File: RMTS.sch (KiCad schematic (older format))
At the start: 49 parts, among them J1 USB_B_Mini, J2 Programmer, J3 Screw_Terminal_01x03, J4 Screw_Terminal_01x04, J5 Screw_Terminal_01x02, J6 Screw_Terminal_01x02, J8 CONN_03, Q1 PMV20ENR, U1 ADP2108AUJ-3.3, U2 MK20DX256VLH7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

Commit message: Fixed rescued symbols
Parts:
- JP1: symbol RMTS-rescue:XBEE-SparkFun-RF -> SparkFun-RF:XBEE
- U2: symbol RMTS-rescue:MK20DX256VLH7-Mine -> Mine:MK20DX256VLH7
- U3: symbol RMTS-rescue:ADS1219-Mine -> Mine:ADS1219
- U4: symbol RMTS-rescue:MCP6N11-Mine -> Mine:MCP6N11
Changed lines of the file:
@@
 $EndDescr
 $Comp
-L RMTS-rescue:MK20DX256VLH7-Mine U2
+L Mine:MK20DX256VLH7 U2
 U 1 1 5D344F89
 P 9450 1500
@@
 Connection ~ 6800 4100
 $Comp
-L RMTS-rescue:ADS1219-Mine U3
+L Mine:ADS1219 U3
 U 1 1 5D3AE65D
 P 3650 6800
@@
 $EndComp
 $Comp
-L RMTS-rescue:MCP6N11-Mine U4
+L Mine:MCP6N11 U4
 U 1 1 5D4392E2
 P 3650 8100
@@
 $EndComp
 $Comp
-L RMTS-rescue:XBEE-SparkFun-RF JP1
+L SparkFun-RF:XBEE JP1
 U 1 1 5D38660F
 P 9500 7900

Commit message: Fixed broken header
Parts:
- J8: symbol RMTS-rescue:CONN_03-SparkFun-Connectors -> SparkFun-Connectors:CONN_03
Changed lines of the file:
@@
 $EndComp
 $Comp
-L RMTS-rescue:CONN_03-SparkFun-Connectors J8
+L SparkFun-Connectors:CONN_03 J8
 U 1 1 5D6FAE37
 P 12550 4900

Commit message: Fixed older microSD footprint
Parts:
- J?: footprint Connectors_Hirose:microSD_Card_Receptacle_Hirose_DM3AT-SF-PEJM5 -> Connector_Card:microSD_HC_Hirose_DM3AT-SF-PEJM5
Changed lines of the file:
@@
 F 0 "J?" H 13900 3100 50  0000 C CNN
 F 1 "Micro_SD_Card_Det_Hirose_DM3AT" H 13900 3000 50  0000 C CNN
-F 2 "Connectors_Hirose:microSD_Card_Receptacle_Hirose_DM3AT-SF-PEJM5" H 16000 2950 50  0001 C CNN
+F 2 "Connector_Card:microSD_HC_Hirose_DM3AT-SF-PEJM5" H 16000 2950 50  0001 C CNN
 F 3 "https://www.hirose.com/product/en/download_file/key_name/DM3/category/Catalog/doc_file_id/49662/?file_category_id=4&item_id=195&is_series=1" H 13950 2350 50  0001 C CNN
 	1    13950 2250

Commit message: Finished layout
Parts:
- added J10, J9: CONN_02, Connectors:1X02, symbol SparkFun-Connectors:CONN_02
- gave numbers to parts that had none: 5
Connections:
- net at D2.2 (A), J6.2 (Pin_2), Q1.3 (D)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: now also J10.1
- net at D1.2 (A), J6.1 (Pin_1), J8.2: now also J9.2
- net at D2.1 (K), R10.1: now also J10.2
- net at D1.1 (K), R9.1: now also J9.1
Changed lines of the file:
@@
 	12650 5000 12650 5450
 Wire Wire Line
-	12650 5450 13500 5450
+	12650 5450 13250 5450
 Wire Wire Line
 	12750 5000 12750 5200
@@
 	12550 5200 12550 5000
 $Comp
-L Device:C C?
+L Device:C C14
 U 1 1 5D457490
 P 7350 3450
-F 0 "C?" V 7200 3300 50  0000 L CNN
+F 0 "C14" V 7200 3300 50  0000 L CNN
 F 1 "12pF" V 7200 3450 50  0000 L CNN
 F 2 "Capacitor_SMD:C_0805_2012Metric_Pad1.15x1.40mm_HandSolder" H 7388 3300 50  0001 C CNN
@@
 $EndComp
 $Comp
-L Device:C C?
+L Device:C C15
 U 1 1 5D45849D
 P 7350 3750
-F 0 "C?" V 7200 3600 50  0000 L CNN
+F 0 "C15" V 7200 3600 50  0000 L CNN
 F 1 "12pF" V 7200 3750 50  0000 L CNN
 F 2 "Capacitor_SMD:C_0805_2012Metric_Pad1.15x1.40mm_HandSolder" H 7388 3600 50  0001 C CNN
@@
 Connection ~ 7700 3450
 $Comp
-L power:GND #PWR?
+L power:GND #PWR0131
 U 1 1 5D46BD2D
 P 7100 3850
-F 0 "#PWR?" H 7100 3600 50  0001 C CNN
+F 0 "#PWR0131" H 7100 3600 50  0001 C CNN
 F 1 "GND" H 7105 3677 50  0000 C CNN
 F 2 "" H 7100 3850 50  0001 C CNN
@@
 XTAL2
 $Comp
-L Device:Crystal_GND24_Small Y?
+L Device:Crystal_GND24_Small Y2
 U 1 1 5D4A38E4
 P 5400 3600
-F 0 "Y?" V 5350 3750 50  0000 L CNN
+F 0 "Y2" V 5350 3750 50  0000 L CNN
 F 1 "Crystal_GND24_Small" V 5400 3750 50  0000 L CNN
 F 2 "Crystal:Crystal_SMD_3225-4Pin_3.2x2.5mm" H 5400 3600 50  0001 C CNN
@@
 	5400 3700 5400 3750
 $Comp
-L power:GND #PWR?
+L power:GND #PWR0132
 U 1 1 5D4B952D
 P 5550 3850
-F 0 "#PWR?" H 5550 3600 50  0001 C CNN
+F 0 "#PWR0132" H 5550 3600 50  0001 C CNN
 F 1 "GND" H 5555 3677 50  0000 C CNN
 F 2 "" H 5550 3850 50  0001 C CNN
@@
 NoConn ~ 13050 2750
 $Comp
-L Connector:Micro_SD_Card_Det_Hirose_DM3AT J?
+L Connector:Micro_SD_Card_Det_Hirose_DM3AT J7
 U 1 1 5D5BC0CE
 P 13950 2250
-F 0 "J?" H 13900 3100 50  0000 C CNN
+F 0 "J7" H 13900 3100 50  0000 C CNN
 F 1 "Micro_SD_Card_Det_Hirose_DM3AT" H 13900 3000 50  0000 C CNN
 F 2 "Connector_Card:microSD_HC_Hirose_DM3AT-SF-PEJM5" H 16000 2950 50  0001 C CNN
@@
 $EndComp
 $Comp
-L power:+3.3V #PWR?
+L power:+3.3V #PWR0137
 U 1 1 5D5BEC27
 P 13000 1700
-F 0 "#PWR?" H 13000 1550 50  0001 C CNN
+F 0 "#PWR0137" H 13000 1550 50  0001 C CNN
 F 1 "+3.3V" H 13015 1873 50  0000 C CNN
 F 2 "" H 13000 1700 50  0001 C CNN
@@
 	13000 2150 13050 2150
 $Comp
-L power:GND #PWR?
+L power:GND #PWR0138
 U 1 1 5D5D5D6B
 P 13000 3000
-F 0 "#PWR?" H 13000 2750 50  0001 C CNN
+F 0 "#PWR0138" H 13000 2750 50  0001 C CNN
 F 1 "GND" H 13005 2827 50  0000 C CNN
 F 2 "" H 13000 3000 50  0001 C CNN
@@
 	13000 2350 13050 2350
 $Comp
-L power:GND #PWR?
+L power:GND #PWR0139
 U 1 1 5D5EDA99
 P 14800 3000
-F 0 "#PWR?" H 14800 2750 50  0001 C CNN
+F 0 "#PWR0139" H 14800 2750 50  0001 C CNN
 F 1 "GND" H 14805 2827 50  0000 C CNN
 F 2 "" H 14800 3000 50  0001 C CNN
@@
 	14800 2750 14800 3000
 $Comp
-L power:+3.3V #PWR?
+L power:+3.3V #PWR0140
 U 1 1 5D5FA187
 P 12250 2150
-F 0 "#PWR?" H 12250 2000 50  0001 C CNN
+F 0 "#PWR0140" H 12250 2000 50  0001 C CNN
 F 1 "+3.3V" H 12265 2323 50  0000 C CNN
 F 2 "" H 12250 2150 50  0001 C CNN
@@
 $EndComp
 $Comp
-L Device:C C?
+L Device:C C16
 U 1 1 5D5FA667
 P 12250 2350
-F 0 "C?" H 12365 2396 50  0000 L CNN
+F 0 "C16" H 12365 2396 50  0000 L CNN
 F 1 "0.1uF" H 12365 2305 50  0000 L CNN
 F 2 "Capacitor_SMD:C_0805_2012Metric_Pad1.15x1.40mm_HandSolder" H 12288 2200 50  0001 C CNN
@@
 	12250 2200 12250 2150
 $Comp
-L power:GND #PWR?
+L power:GND #PWR0141
 U 1 1 5D607314
 P 12250 2550
-F 0 "#PWR?" H 12250 2300 50  0001 C CNN
+F 0 "#PWR0141" H 12250 2300 50  0001 C CNN
 F 1 "GND" H 12255 2377 50  0000 C CNN
 F 2 "" H 12250 2550 50  0001 C CNN
@@
 NoConn ~ 10200 8300
 NoConn ~ 10200 8400
+$Comp
+L SparkFun-Connectors:CONN_02 J9
+U 1 1 5D4ED64B
+P 13150 5700
+F 0 "J9" H 13108 6110 45  0000 C CNN
+F 1 "CONN_02" H 13108 6026 45  0000 C CNN
+F 2 "Connectors:1X02" H 13150 5950 20  0001 C CNN
+F 3 "" H 13150 5700 50  0001 C CNN
+F 4 "XXX-00000" H 13108 5931 60  0000 C CNN "Field4"
+	1    13150 5700
+	1    0    0    -1
+$EndComp
+$Comp
+L SparkFun-Connectors:CONN_02 J10
+U 1 1 5D4EE378
+P 15300 5650
+F 0 "J10" H 15072 5605 45  0000 R CNN
+F 1 "CONN_02" H 15072 5689 45  0000 R CNN
+F 2 "Connectors:1X02" H 15300 5900 20  0001 C CNN
+F 3 "" H 15300 5650 50  0001 C CNN
+F 4 "XXX-00000" H 15072 5784 60  0000 R CNN "Field4"
+	1    15300 5650
+	-1   0    0    1
+$EndComp
+Wire Wire Line
+	13500 5450 13250 5450
+Wire Wire Line
+	13250 5450 13250 5600
+Connection ~ 13250 5450
+Wire Wire Line
+	13250 5700 13350 5700
+Wire Wire Line
+	13350 5700 13350 5750
+Wire Wire Line
+	13350 5750 13500 5750
+Connection ~ 13500 5750
+Wire Wire Line
+	14650 5650 15200 5650
+Connection ~ 14650 5650
+Wire Wire Line
+	15200 5750 15200 5950
+Wire Wire Line
+	15200 5950 14650 5950
+Connection ~ 14650 5950
 $EndSCHEMATC

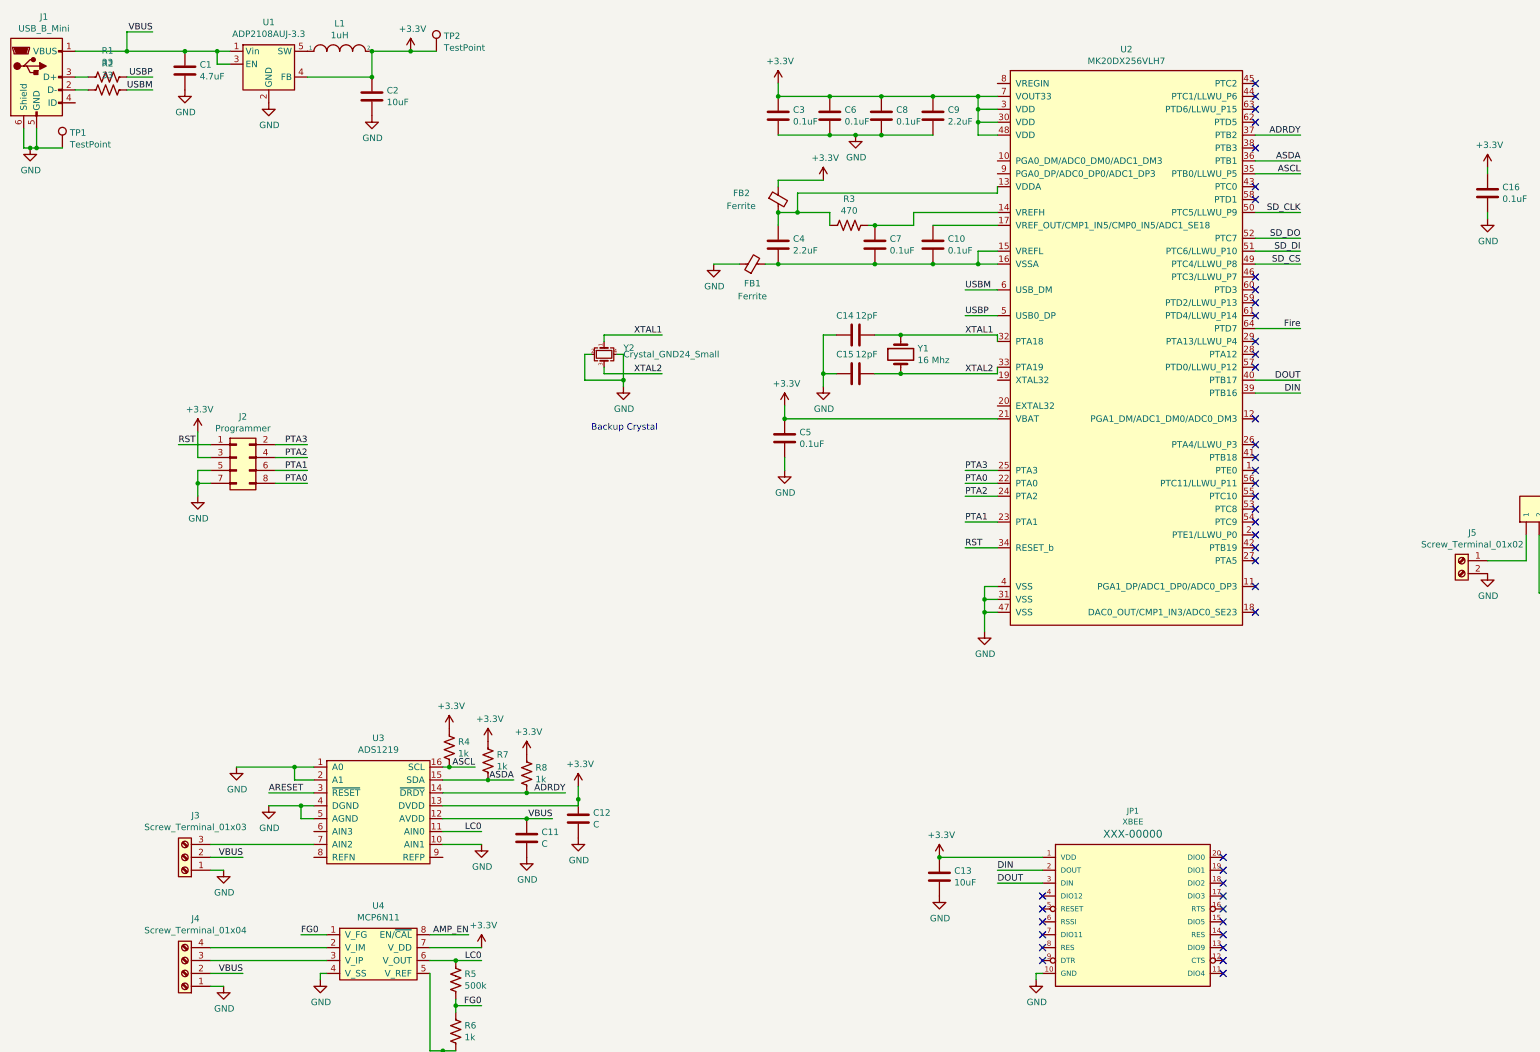
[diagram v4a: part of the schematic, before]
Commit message: Changed USB to full size, connected amp enable, cleaned up routing
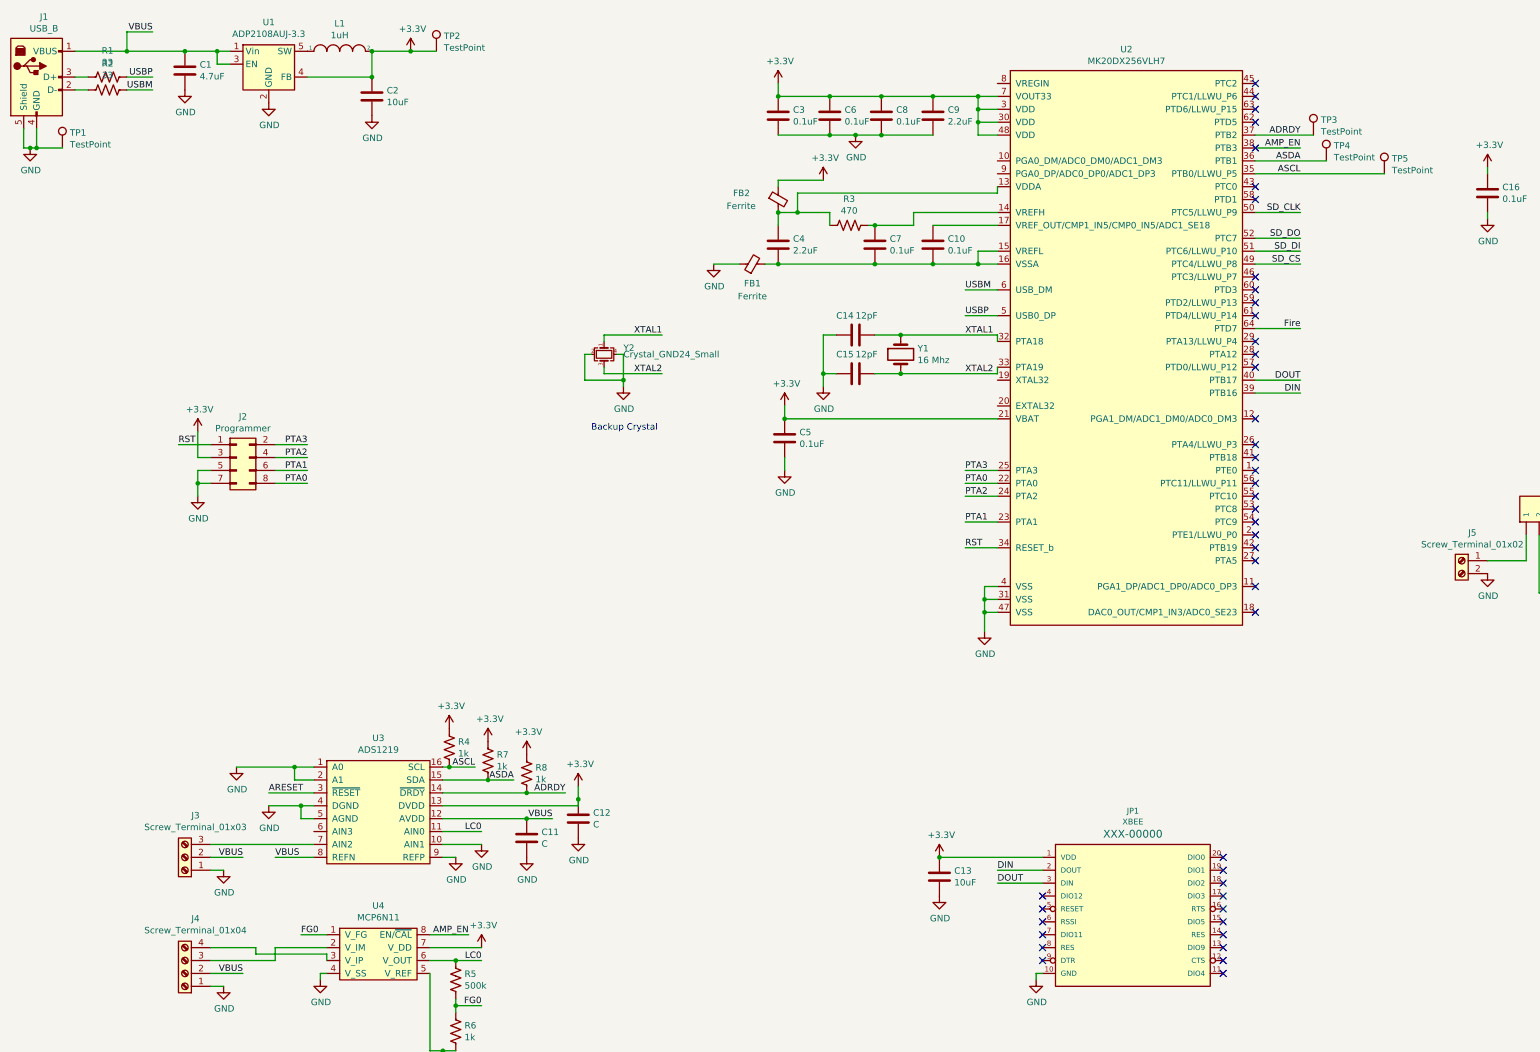
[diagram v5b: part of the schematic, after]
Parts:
- removed J1: USB_B_Mini, Connector_USB:USB_Micro-B_Molex_47346-0001, symbol Connector:USB_B_Mini
- added J1: USB_B, Connector_USB:USB_B_OST_USB-B1HSxx_Horizontal, symbol Connector:USB_B
- added TP3, TP4, TP5: TestPoint, TestPoint:TestPoint_THTPad_1.0x1.0mm_Drill0.5mm, symbol Connector:TestPoint
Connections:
- net ADRDY: now also TP3.1
- net AMP_EN: now also U2.38 (PTB3)
- net ASCL: now also TP5.1
- net ASDA: now also TP4.1
- net GND: now also U3.9 (REFP), J1.4 (GND), J1.5 (Shield)
- net VBUS: now also U3.8 (REFN), J1.1 (VBUS)
- net at R2.2: now also J1.2 (D-)
- net at R1.2: now also J1.3 (D+)
- net at J4.3 (Pin_3): now also U4.2 (V_IM); no longer U4.3 (V_IP)
- net at J4.4 (Pin_4): now also U4.3 (V_IP); no longer U4.2 (V_IM)
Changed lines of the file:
@@
 	8350 5600 8350 5750
-$Comp
-L Connector:USB_B_Mini J1
-U 1 1 5D34B736
-P 1000 1450
-F 0 "J1" H 1057 1917 50  0000 C CNN
-F 1 "USB_B_Mini" H 1057 1826 50  0000 C CNN
-F 2 "Connector_USB:USB_Micro-B_Molex_47346-0001" H 1150 1400 50  0001 C CNN
-F 3 "~" H 1150 1400 50  0001 C CNN
-	1    1000 1450
-	1    0    0    -1
-$EndComp
 $Comp
 L power:GND #PWR0102
@@
 Wire Wire Line
 	2800 7100 3050 7100
-Wire Wire Line
-	10450 2200 10800 2200
 Text Label 10800 2200 2    50   ~ 0
 ASCL
-Wire Wire Line
-	10450 2100 10800 2100
 Text Label 10800 2100 2    50   ~ 0
 ASDA
-Wire Wire Line
-	10450 1900 10800 1900
 Text Label 10800 1900 2    50   ~ 0
 ADRDY
@@
 	4150 9000 4250 9000
 Wire Wire Line
-	2350 8300 3250 8300
-Wire Wire Line
-	2350 8200 3250 8200
-Wire Wire Line
 	4150 7400 4450 7400
-$Comp
-L power:GND #PWR0127
-U 1 1 5D55CA4C
-P 4450 7400
-F 0 "#PWR0127" H 4450 7150 50  0001 C CNN
-F 1 "GND" H 4455 7227 50  0000 C CNN
-F 2 "" H 4450 7400 50  0001 C CNN
-F 3 "" H 4450 7400 50  0001 C CNN
-	1    4450 7400
-	1    0    0    -1
-$EndComp
 $Comp
 L SparkFun-RF:XBEE JP1
@@
 	15200 5950 14650 5950
 Connection ~ 14650 5950
+Wire Wire Line
+	3150 7500 2850 7500
+Text Label 2850 7500 0    50   ~ 0
+VBUS
+$Comp
+L power:GND #PWR0127
+U 1 1 5D55CA4C
+P 4450 7400
+F 0 "#PWR0127" H 4450 7150 50  0001 C CNN
+F 1 "GND" H 4455 7227 50  0000 C CNN
+F 2 "" H 4450 7400 50  0001 C CNN
+F 3 "" H 4450 7400 50  0001 C CNN
+	1    4450 7400
+	1    0    0    -1
+$EndComp
+$Comp
+L power:GND #PWR0142
+U 1 1 5D645680
+P 4250 7500
+F 0 "#PWR0142" H 4250 7250 50  0001 C CNN
+F 1 "GND" H 4255 7327 50  0000 C CNN
+F 2 "" H 4250 7500 50  0001 C CNN
+F 3 "" H 4250 7500 50  0001 C CNN
+	1    4250 7500
+	1    0    0    -1
+$EndComp
+Wire Wire Line
+	4150 7500 4250 7500
+Wire Wire Line
+	2350 8300 2850 8300
+Wire Wire Line
+	2850 8300 2850 8200
+Wire Wire Line
+	2850 8200 3250 8200
+Wire Wire Line
+	2350 8200 2700 8200
+Wire Wire Line
+	2700 8200 2700 8250
+Wire Wire Line
+	3250 8250 3250 8300
+Wire Wire Line
+	2700 8250 3250 8250
+Wire Wire Line
+	10450 2000 10800 2000
+Text Label 10800 2000 2    50   ~ 0
+AMP_EN
+$Comp
+L Connector:USB_B J1
+U 1 1 5D732327
+P 1000 1450
+F 0 "J1" H 1057 1917 50  0000 C CNN
+F 1 "USB_B" H 1057 1826 50  0000 C CNN
+F 2 "Connector_USB:USB_B_OST_USB-B1HSxx_Horizontal" H 1150 1400 50  0001 C CNN
+F 3 " ~" H 1150 1400 50  0001 C CNN
+	1    1000 1450
+	1    0    0    -1
+$EndComp
+$Comp
+L Connector:TestPoint TP3
+U 1 1 5D79BB5E
+P 10900 1900
+F 0 "TP3" H 10958 2018 50  0000 L CNN
+F 1 "TestPoint" H 10958 1927 50  0000 L CNN
+F 2 "TestPoint:TestPoint_THTPad_1.0x1.0mm_Drill0.5mm" H 11100 1900 50  0001 C CNN
+F 3 "~" H 11100 1900 50  0001 C CNN
+	1    10900 1900
+	1    0    0    -1
+$EndComp
+$Comp
+L Connector:TestPoint TP4
+U 1 1 5D79EB42
+P 11000 2100
+F 0 "TP4" H 11058 2218 50  0000 L CNN
+F 1 "TestPoint" H 11058 2127 50  0000 L CNN
+F 2 "TestPoint:TestPoint_THTPad_1.0x1.0mm_Drill0.5mm" H 11200 2100 50  0001 C CNN
+F 3 "~" H 11200 2100 50  0001 C CNN
+	1    11000 2100
+	1    0    0    -1
+$EndComp
+$Comp
+L Connector:TestPoint TP5
+U 1 1 5D79F9A3
+P 11450 2200
+F 0 "TP5" H 11508 2318 50  0000 L CNN
+F 1 "TestPoint" H 11508 2227 50  0000 L CNN
+F 2 "TestPoint:TestPoint_THTPad_1.0x1.0mm_Drill0.5mm" H 11650 2200 50  0001 C CNN
+F 3 "~" H 11650 2200 50  0001 C CNN
+	1    11450 2200
+	1    0    0    -1
+$EndComp
+Wire Wire Line
+	10450 1900 10900 1900
+Wire Wire Line
+	10450 2100 11000 2100
+Wire Wire Line
+	10450 2200 11450 2200
 $EndSCHEMATC

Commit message: Fixed mistakes
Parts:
- C11, C12: value C -> 0.1uF
- R10, R9: value R_US -> 1k
- TP1: value TestPoint -> GND
- TP2: value TestPoint -> 3V3
- TP3: value TestPoint -> DRDY
- TP4: value TestPoint -> SDA
- TP5: value TestPoint -> SCL
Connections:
- net GND: now also U3.8 (REFN); no longer U3.9 (REFP)
- net VBUS: now also U3.9 (REFP); no longer U3.8 (REFN)
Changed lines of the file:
@@
 P 4100 1250
 F 0 "TP2" H 4158 1368 50  0000 L CNN
-F 1 "TestPoint" H 4158 1277 50  0000 L CNN
+F 1 "3V3" H 4158 1277 50  0000 L CNN
 F 2 "TestPoint:TestPoint_THTPad_2.0x2.0mm_Drill1.0mm" H 4300 1250 50  0001 C CNN
 F 3 "~" H 4300 1250 50  0001 C CNN
@@
 P 1200 2000
 F 0 "TP1" H 1258 2118 50  0000 L CNN
-F 1 "TestPoint" H 1258 2027 50  0000 L CNN
+F 1 "GND" H 1258 2027 50  0000 L CNN
 F 2 "TestPoint:TestPoint_THTPad_2.0x2.0mm_Drill1.0mm" H 1400 2000 50  0001 C CNN
 F 3 "~" H 1400 2000 50  0001 C CNN
@@
 P 4800 7350
 F 0 "C11" H 4915 7396 50  0000 L CNN
-F 1 "C" H 4915 7305 50  0000 L CNN
+F 1 "0.1uF" H 4915 7305 50  0000 L CNN
 F 2 "Capacitor_SMD:C_0805_2012Metric_Pad1.15x1.40mm_HandSolder" H 4838 7200 50  0001 C CNN
 F 3 "~" H 4800 7350 50  0001 C CNN
@@
 P 5200 7200
 F 0 "C12" H 5315 7246 50  0000 L CNN
-F 1 "C" H 5315 7155 50  0000 L CNN
+F 1 "0.1uF" H 5315 7155 50  0000 L CNN
 F 2 "Capacitor_SMD:C_0805_2012Metric_Pad1.15x1.40mm_HandSolder" H 5238 7050 50  0001 C CNN
 F 3 "~" H 5200 7200 50  0001 C CNN
@@
 P 14650 6100
 F 0 "R10" H 14718 6146 50  0000 L CNN
-F 1 "R_US" H 14718 6055 50  0000 L CNN
+F 1 "1k" H 14718 6055 50  0000 L CNN
 F 2 "Resistor_SMD:R_0805_2012Metric_Pad1.15x1.40mm_HandSolder" V 14690 6090 50  0001 C CNN
 F 3 "~" H 14650 6100 50  0001 C CNN
@@
 P 13500 5900
 F 0 "R9" H 13568 5946 50  0000 L CNN
-F 1 "R_US" H 13568 5855 50  0000 L CNN
+F 1 "1k" H 13568 5855 50  0000 L CNN
 F 2 "Resistor_SMD:R_0805_2012Metric_Pad1.15x1.40mm_HandSolder" V 13540 5890 50  0001 C CNN
 F 3 "~" H 13500 5900 50  0001 C CNN
@@
 Wire Wire Line
 	3150 7500 2850 7500
-Text Label 2850 7500 0    50   ~ 0
+Text Label 4350 7500 2    50   ~ 0
 VBUS
 $Comp
@@
 L power:GND #PWR0142
 U 1 1 5D645680
-P 4250 7500
-F 0 "#PWR0142" H 4250 7250 50  0001 C CNN
-F 1 "GND" H 4255 7327 50  0000 C CNN
-F 2 "" H 4250 7500 50  0001 C CNN
-F 3 "" H 4250 7500 50  0001 C CNN
-	1    4250 7500
-	1    0    0    -1
-$EndComp
-Wire Wire Line
-	4150 7500 4250 7500
+P 2850 7500
+F 0 "#PWR0142" H 2850 7250 50  0001 C CNN
+F 1 "GND" H 2855 7327 50  0000 C CNN
+F 2 "" H 2850 7500 50  0001 C CNN
+F 3 "" H 2850 7500 50  0001 C CNN
+	1    2850 7500
+	1    0    0    -1
+$EndComp
 Wire Wire Line
 	2350 8300 2850 8300
@@
 P 10900 1900
 F 0 "TP3" H 10958 2018 50  0000 L CNN
-F 1 "TestPoint" H 10958 1927 50  0000 L CNN
+F 1 "DRDY" H 10958 1927 50  0000 L CNN
 F 2 "TestPoint:TestPoint_THTPad_1.0x1.0mm_Drill0.5mm" H 11100 1900 50  0001 C CNN
 F 3 "~" H 11100 1900 50  0001 C CNN
@@
 P 11000 2100
 F 0 "TP4" H 11058 2218 50  0000 L CNN
-F 1 "TestPoint" H 11058 2127 50  0000 L CNN
+F 1 "SDA" H 11058 2127 50  0000 L CNN
 F 2 "TestPoint:TestPoint_THTPad_1.0x1.0mm_Drill0.5mm" H 11200 2100 50  0001 C CNN
 F 3 "~" H 11200 2100 50  0001 C CNN
@@
 P 11450 2200
 F 0 "TP5" H 11508 2318 50  0000 L CNN
-F 1 "TestPoint" H 11508 2227 50  0000 L CNN
+F 1 "SCL" H 11508 2227 50  0000 L CNN
 F 2 "TestPoint:TestPoint_THTPad_1.0x1.0mm_Drill0.5mm" H 11650 2200 50  0001 C CNN
 F 3 "~" H 11650 2200 50  0001 C CNN
@@
 Wire Wire Line
 	10450 2200 11450 2200
+Wire Wire Line
+	4150 7500 4350 7500
 $EndSCHEMATC
